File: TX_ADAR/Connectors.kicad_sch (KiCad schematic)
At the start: 4 parts, among them J1 Conn_Coaxial, J11 RJ45_LED_Shielded, J12 RJ45_LED_Shielded, J2 Conn_Coaxial

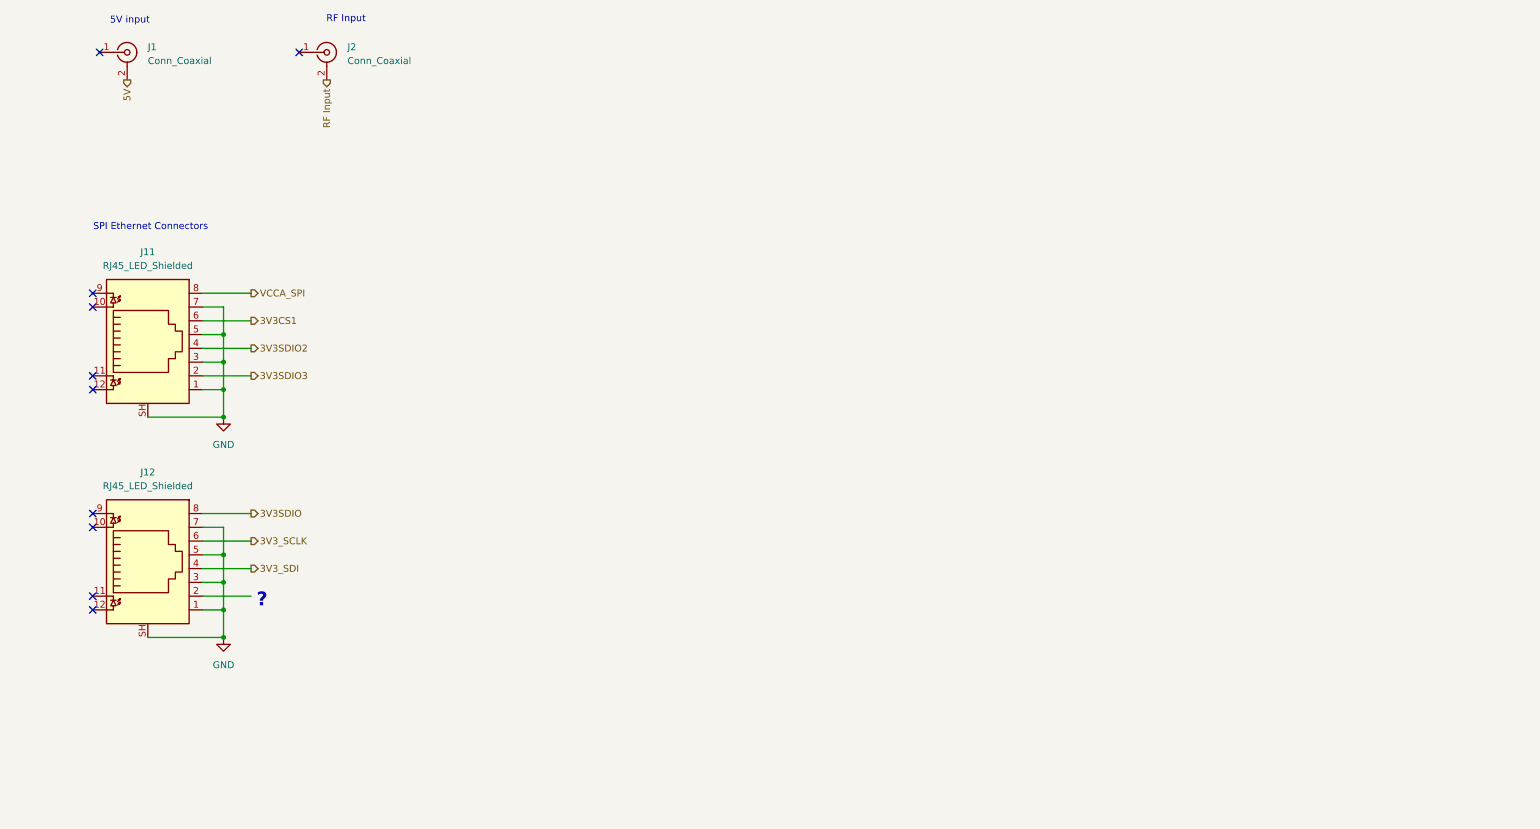
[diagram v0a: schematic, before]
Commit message: After Vccb>Vcca
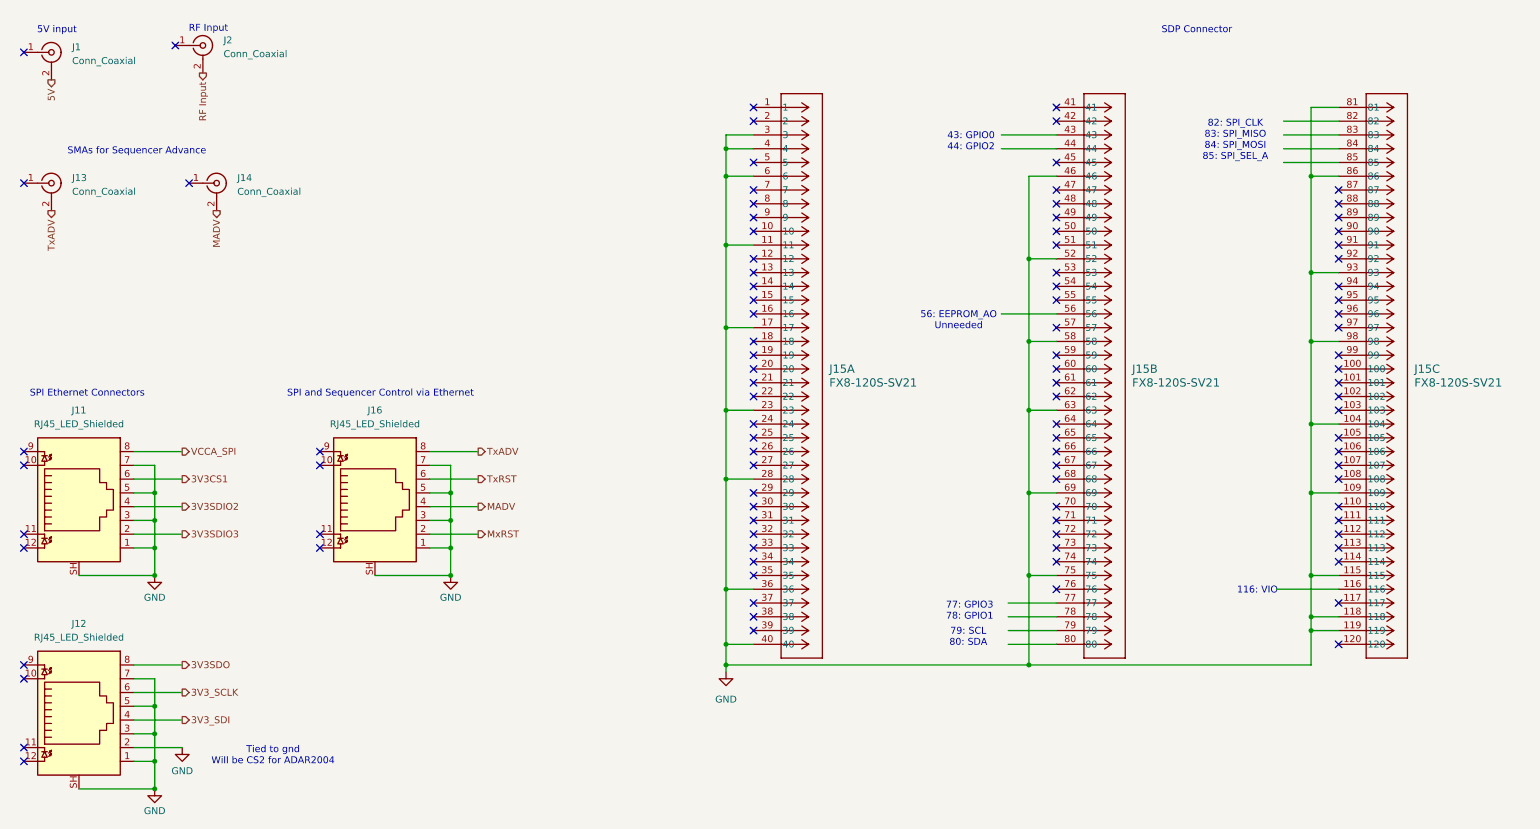
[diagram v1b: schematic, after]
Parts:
- added J13, J14: Conn_Coaxial, symbol Connector:Conn_Coaxial
- added J15: FX8-120S-SV21, CONN120_FX8-120S-SV_HIR, symbol 2026-08-26_15-47-23:FX8-120S-SV21
- added J16: RJ45_LED_Shielded, symbol Connector:RJ45_LED_Shielded
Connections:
- net GND: now also J12.2, J15.104, J15.109, J15.11, J15.115, J15.118, J15.119, J15.17, J15.23, J15.28, J15.3, J15.36, J15.4, J15.40, J15.46, J15.52, J15.58, J15.6, J15.63, J15.69, J15.75, J15.81, J15.86, J15.93, J15.98, J16.1, J16.3, J16.5, J16.7, J16.SH
- net 3V3SDIO renamed 3V3SDO
- new net MADV: J14.2 (Ext), J16.4
- new net MxRST: J16.2
- new net TxADV: J13.2 (Ext), J16.8
- new net TxRST: J16.6
- no-connect marks 10 -> 100
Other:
- note added: "116: VIO"
- note added: "43: GPIO0 44: GPIO2"
- note added: "56: EEPROM_AO"
- note added: "77: GPIO3 78: GPIO1"
- note added: "79: SCL 80: SDA"
- note added: "82: SPI_CLK 83: SPI_MISO 84: SPI_MOSI 85: SPI_SEL_A"
- note added: "SDP Connector"
- note added: "SMAs for Sequencer Advance"
- note added: "SPI and Sequencer Control via Ethernet"
- note added: "Tied to gnd Will be CS2 for ADAR2004"
- note added: "Unneeded"
- note removed: "?"
- moved on the sheet: J1, J11, J12, J2

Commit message: Moving things around
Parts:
- added J17, J18: Conn_Coaxial, symbol Connector:Conn_Coaxial
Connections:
- net 3V3CS1 is gone; now on net 3V3CSB: J11.6
- net 3V3_SDI is gone; now on net 3V3_SDIO: J12.4
- net MxRST is gone; now on net MRST: J16.2
- net 3V3SDO: now also J15.83
- net 3V3_SCLK: now also J15.82
- net MADV: now also J15.44
- net TxADV: now also J15.43
- net TxRST: now also J15.78, J17.2 (Ext)
- net VCCA_SPI: now also J15.116
- net 3V3_SDIO: now reaches J15.84
- net 3V3CSB: now reaches J15.85
- net MRST: now reaches J15.77
- net MRST: now also J18.2 (Ext)
- no-connect marks 100 -> 105
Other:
- note added: "116: VIO (3V3)"
- note added: "Ask about SDIO and SDIO2-3"
- note added: "Tied to gnd Will be CSB2 for ADAR2004"
- note removed: "116: VIO"
- note removed: "Tied to gnd Will be CS2 for ADAR2004"
- moved on the sheet: J11, J12, J13, J14, J15A, J15B, J15C, J16
